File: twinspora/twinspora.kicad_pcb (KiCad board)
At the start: 2 copper layers, 81 parts, among them J1 XY-SH1_0-4A61, J2 TYPE-C-31-M-12, J3 XY-SH1_0-6A51, J4 XY-SH1_0-6A51, J5 XY-XH2_54-2A21, J6 XY-XH2_54-2A21, J7 XY-XH2_54-3A11, Q1 AO3401A, U1 STM32G473RBTx, U10 DRV8316CRRGFR, U2 MT6701QT, U3 MT6701QT, U5 DRV8316CRRGFR, U6 TS1187A26020, U7 CA-IF1044VD-Q1, U8 XC6206P332MR, U9 TS1187A26020, X2 X322512MSB4SI

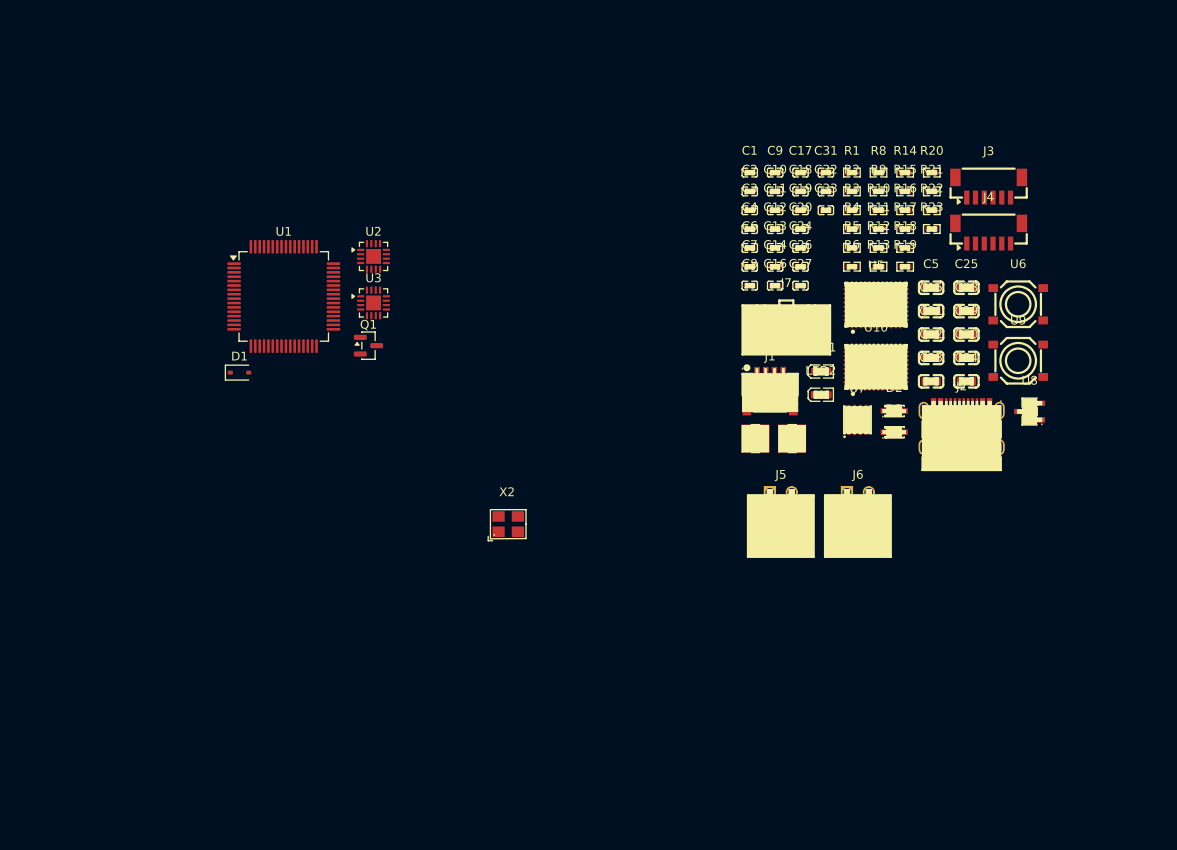
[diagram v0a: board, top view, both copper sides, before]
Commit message: added smt nut
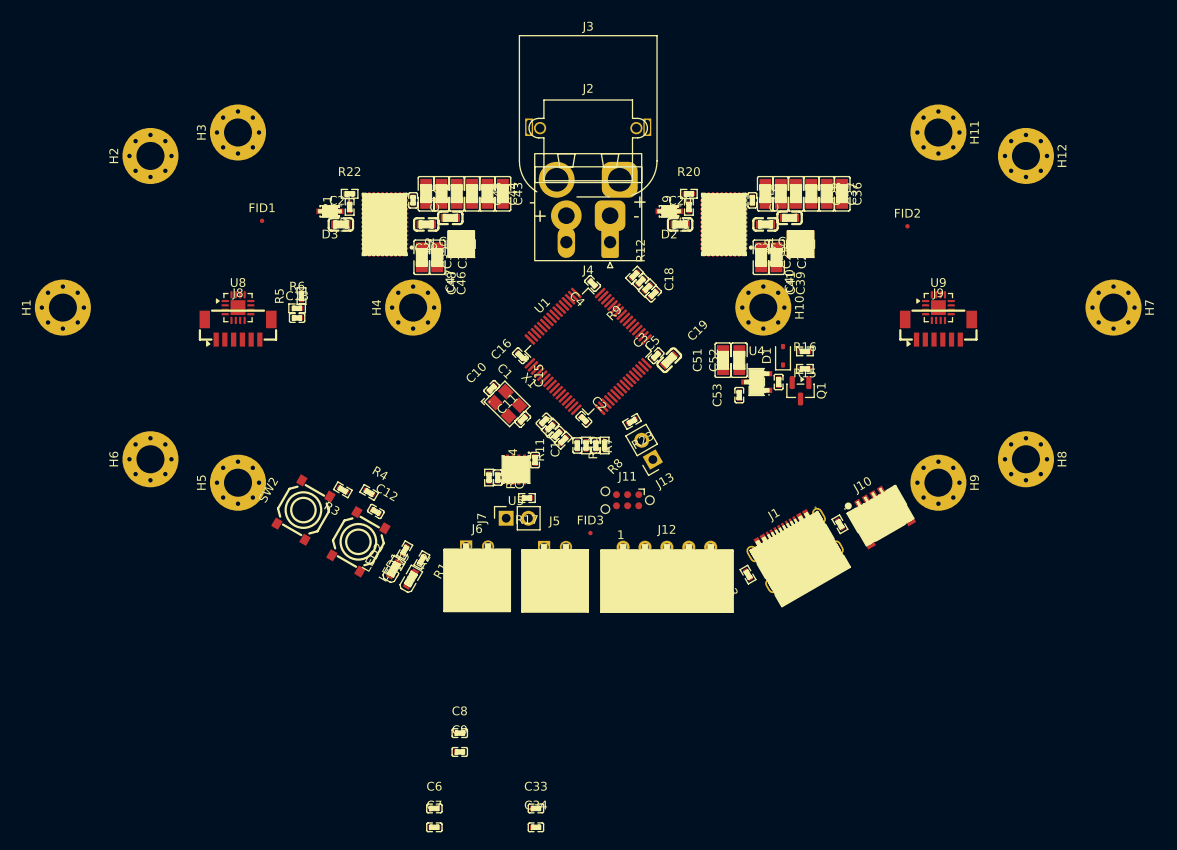
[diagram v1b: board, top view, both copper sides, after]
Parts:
- removed U10: DRV8316CRRGFR, Motor_Driver:VQFN-40_L7.0-W5.0-P0.50-BL-EP5.7
- removed U2, U3: MT6701QT, Package_DFN_QFN:QFN-16-1EP_3x3mm_P0.5mm_EP1.7x1.7mm
- removed X2: X322512MSB4SI, Oscillator:X322512MSB4SI
- added C35: CL05B104KB54PNC, Basic_Capacitors_Resistors:C0402, F.Cu at (158.7, 87.8)
- added C36: GRM21BR61H106KE43L, Basic_Capacitors_Resistors:C0805, F.Cu at (169.0, 87.0)
- added C37: GRM21BR61H106KE43L, Basic_Capacitors_Resistors:C0805, F.Cu at (167.2, 87.0)
- added C38: GRM21BR61H106KE43L, Basic_Capacitors_Resistors:C0805, F.Cu at (165.5, 87.0)
- added C39: GRM21BR61H106KE43L, Basic_Capacitors_Resistors:C0805, F.Cu at (163.7, 87.0)
- added C40: GRM21BR61H106KE43L, Basic_Capacitors_Resistors:C0805, F.Cu at (162.0, 87.0)
- added C41: GRM21BR61H106KE43L, Basic_Capacitors_Resistors:C0805, F.Cu at (160.2, 87.0)
- added C42: CL05B104KB54PNC, Basic_Capacitors_Resistors:C0402, F.Cu at (120.0, 87.8)
- added C43: GRM21BR61H106KE43L, Basic_Capacitors_Resistors:C0805, F.Cu at (130.2, 87.0)
- added C44: GRM21BR61H106KE43L, Basic_Capacitors_Resistors:C0805, F.Cu at (128.5, 87.0)
- added C45: GRM21BR61H106KE43L, Basic_Capacitors_Resistors:C0805, F.Cu at (126.7, 87.0)
- added C46: GRM21BR61H106KE43L, Basic_Capacitors_Resistors:C0805, F.Cu at (125.0, 87.0)
- added C47: GRM21BR61H106KE43L, Basic_Capacitors_Resistors:C0805, F.Cu at (123.2, 87.0)
- added C48: GRM21BR61H106KE43L, Basic_Capacitors_Resistors:C0805, F.Cu at (121.5, 87.0)
- added C51: GRM21BR61H106KE43L, Basic_Capacitors_Resistors:C0805, F.Cu at (155.4, 106.0)
- added C52: GRM21BR61H106KE43L, Basic_Capacitors_Resistors:C0805, F.Cu at (157.3, 106.0)
- added C53: CL05B104KB54PNC, Basic_Capacitors_Resistors:C0402, F.Cu at (157.2, 110.0)
- added FID1: Fiducial, Fiducial:Fiducial_0.5mm_Mask1mm, F.Cu at (102.7, 90.1)
- added FID2: Fiducial, Fiducial:Fiducial_0.5mm_Mask1mm, F.Cu at (176.5, 90.7)
- added FID3: Fiducial, Fiducial:Fiducial_0.5mm_Mask1mm, F.Cu at (140.2, 125.8)
- added H1: MountingHole_Pad, MountingHole:MountingHole_3.2mm_M3_Pad_Via, F.Cu at (80.0, 100.0)
- added H10: MountingHole_Pad, MountingHole:MountingHole_3.2mm_M3_Pad_Via, F.Cu at (160.0, 100.0)
- added H11: MountingHole_Pad, MountingHole:MountingHole_3.2mm_M3_Pad_Via, F.Cu at (180.0, 80.0)
- added H12: MountingHole_Pad, MountingHole:MountingHole_3.2mm_M3_Pad_Via, F.Cu at (190.0, 82.7)
- added H2: MountingHole_Pad, MountingHole:MountingHole_3.2mm_M3_Pad_Via, F.Cu at (90.0, 82.7)
- added H3: MountingHole_Pad, MountingHole:MountingHole_3.2mm_M3_Pad_Via, F.Cu at (100.0, 80.0)
- added H4: MountingHole_Pad, MountingHole:MountingHole_3.2mm_M3_Pad_Via, F.Cu at (120.0, 100.0)
- added H5: MountingHole_Pad, MountingHole:MountingHole_3.2mm_M3_Pad_Via, F.Cu at (100.0, 120.0)
- added H6: MountingHole_Pad, MountingHole:MountingHole_3.2mm_M3_Pad_Via, F.Cu at (90.0, 117.3)
- added H7: MountingHole_Pad, MountingHole:MountingHole_3.2mm_M3_Pad_Via, F.Cu at (200.0, 100.0)
- added H8: MountingHole_Pad, MountingHole:MountingHole_3.2mm_M3_Pad_Via, F.Cu at (190.0, 117.3)
- added H9: MountingHole_Pad, MountingHole:MountingHole_3.2mm_M3_Pad_Via, F.Cu at (180.0, 120.0)
- added J10: XY-SH1_0-4A61, Connector_SH1.0:CONN-SMD_4P-P1.00-WT, F.Cu at (173.2, 123.5)
- added J11: ~, Connector:Tag-Connect_TC2030-IDC-NL, F.Cu at (144.5, 122.0)
- added J12: XY-XH2_54-5A21, Connector_XH2.54:HDR-TH_5P-P2.50-H-F-W7.0-N, F.Cu at (149.0, 127.4)
- added J13: Conn_01x02, Connector_PinSocket_2.54mm:PinSocket_1x02_P2.54mm_Vertical, F.Cu at (147.4, 117.3)
- added J8: XY-SH1_0-6A51, Connector_SH1.0:CONN-SMD_6P-P1.00_XY-SH1.0-6A51, F.Cu at (100.0, 102.5)
- added J9: XY-SH1_0-6A51, Connector_SH1.0:CONN-SMD_6P-P1.00_XY-SH1.0-6A51, F.Cu at (180.0, 102.5)
- added R7: 0402WGF499JTCE, Basic_Capacitors_Resistors:R0402, F.Cu at (139.8, 115.8)
- added SW2: TS1187A26020, Switch:SW-SMD_4P-L5.2-W5.2-1, F.Cu at (107.5, 123.1)
- added SW3: TS1187A26020, Switch:SW-SMD_4P-L5.2-W5.2-1, F.Cu at (113.8, 126.8)
- added U4: XC6206P332MR, Regulator_Linear:SOT-23-3_L2.9-W1.6-P1.90-LS2.8-BR, F.Cu at (159.2, 108.5)
- added X1: X322512MSB4SI, Oscillator:X322512MSB4SI, F.Cu at (130.8, 111.0)
- C10, C11: value CL05B104KB54PNC -> 0402CG200J500NT
- C13, C7, C9: value CL05B104KB54PNC -> CL05A105KA5NQNC
- C14, C6: value CL05A105KA5NQNC -> CL05B103KB5NNNC
- C15: value CL10A226MQ8NRNC -> CL05B103KB5NNNC; footprint Basic_Capacitors_Resistors:C0603 -> Basic_Capacitors_Resistors:C0402
- C16, C17, C18, C19: value CL05B104KB54PNC -> CL05B103KB5NNNC
- C2, C3: value 0402CG200J500NT -> CL05B104KB54PNC
- C20: value CL05A105KA5NQNC -> CL10A105KB8NNNC; footprint Basic_Capacitors_Resistors:C0402 -> Basic_Capacitors_Resistors:C0603
- C21, C30: value CL10A226MQ8NRNC -> CL10A105KB8NNNC
- C22, C23, C34: value CL10A226MQ8NRNC -> CL05B104KB54PNC; footprint Basic_Capacitors_Resistors:C0603 -> Basic_Capacitors_Resistors:C0402
- C24: value CL05A105KA5NQNC -> CL05B104KB54PNC
- C25, C29: value CL10A226MQ8NRNC -> CL10B473KB8NNNC
- C26: value CL05B104KB54PNC -> CL10A105KB8NNNC; footprint Basic_Capacitors_Resistors:C0402 -> Basic_Capacitors_Resistors:C0603
- C27, C31, C32: value CL05A105KA5NQNC -> GRM21BR61H106KE43L; footprint Basic_Capacitors_Resistors:C0402 -> Basic_Capacitors_Resistors:C0805
- C28: value CL10A226MQ8NRNC -> GRM21BR61H106KE43L; footprint Basic_Capacitors_Resistors:C0603 -> Basic_Capacitors_Resistors:C0805
- C4: value CL05B103KB5NNNC -> CL05B104KB54PNC
- D2, D3: value BZT52B5V1S_C19077434 -> BZT52B5V1S
- J1: value XY-SH1_0-4A61 -> TYPE-C-31-M-12; footprint Connector_SH1.0:CONN-SMD_4P-P1.00-WT -> Connector_USB:USB-C_SMD-TYPE-C-31-M-12_1
- J2: value TYPE-C-31-M-12 -> XT30U-M; footprint Connector_USB:USB-C_SMD-TYPE-C-31-M-12_1 -> Connector_AMASS:AMASS_XT30PW-M_1x02_P2.50mm_Horizontal
- J3: value XY-SH1_0-6A51 -> XT60PW-M; footprint Connector_SH1.0:CONN-SMD_6P-P1.00_XY-SH1.0-6A51 -> Connector_AMASS:AMASS_XT60PW-M_1x02_P7.20mm_Horizontal
- J4: value XY-SH1_0-6A51 -> Conn_01x02; footprint Connector_SH1.0:CONN-SMD_6P-P1.00_XY-SH1.0-6A51 -> Connector_Phoenix_MSTB:PhoenixContact_MSTBA_2,5_2-G_1x02_P5.00mm_Horizontal
- J7: value XY-XH2_54-3A11 -> Conn_01x02; footprint Connector_XH2.54:HDR-TH_3P-P2.50-V-F-2 -> Connector_PinSocket_2.54mm:PinSocket_1x02_P2.54mm_Vertical
- LED1: value KT-0603R -> KT-0603W; footprint LED:LED0603-RD -> LED:LED0603-R-RD_WHITE
- LED2: value KT-0603W -> KT-0603R; footprint LED:LED0603-R-RD_WHITE -> LED:LED0603-RD
- R10: value 0402WGF1002TCE -> 0402WGF499JTCE
- R11: value 0402WGF1003TCE -> 0402WGF499JTCE
- R12, R9: value 0402WGF5101TCE -> 0402WGF499JTCE
- R14: value 0402WGF3300TCE -> 0402WGF5101TCE
- R16, R23, R6: value 0402WGF3300TCE -> 0402WGF1002TCE
- R17: value 0402WGF1003TCE -> 0402WGF1200TCE
- R18: value 0402WGF5101TCE -> 0402WGF1002TCE
- R19, R21: value 0402WGF3300TCE -> 0402WGF1003TCE
- R2: value 0402WGF1002TCE -> 0402WGF3300TCE
- R20: value 0402WGF1003TCE -> 0402WGF5101TCE
- R3: value 0402WGF1002TCE -> 0402WGF5101TCE
- R4: value 0402WGF1200TCE -> 0402WGF1002TCE
- R5: value 0402WGF1002TCE -> 0402WGF1003TCE
- R8: value 0402WGF3300TCE -> 0402WGF499JTCE
- U5: value DRV8316CRRGFR -> CA-IF1044VD-Q1; footprint Motor_Driver:VQFN-40_L7.0-W5.0-P0.50-BL-EP5.7 -> Interface_CAN_LIN:DFN-8_L3.0-W3.0-P0.65-BL-EP2.45
- U6: value TS1187A26020 -> DRV8316CRRGFR; footprint Switch:SW-SMD_4P-L5.2-W5.2-1 -> Motor_Driver:VQFN-40_L7.0-W5.0-P0.50-BL-EP5.7
- U7: value CA-IF1044VD-Q1 -> DRV8316CRRGFR; footprint Interface_CAN_LIN:DFN-8_L3.0-W3.0-P0.65-BL-EP2.45 -> Motor_Driver:VQFN-40_L7.0-W5.0-P0.50-BL-EP5.7
- U8: value XC6206P332MR -> MT6701QT; footprint Regulator_Linear:SOT-23-3_L2.9-W1.6-P1.90-LS2.8-BR -> Package_DFN_QFN:QFN-16-1EP_3x3mm_P0.5mm_EP1.7x1.7mm
- U9: value TS1187A26020 -> MT6701QT; footprint Switch:SW-SMD_4P-L5.2-W5.2-1 -> Package_DFN_QFN:QFN-16-1EP_3x3mm_P0.5mm_EP1.7x1.7mm
- moved U8 91.2 mm to (100.0, 100.0)
- moved C33 75.9 mm to (134.0, 157.2)
- moved C9 75.3 mm to (125.3, 150.8)
- moved C7 73.5 mm to (122.4, 159.4)
- moved C6 73.5 mm to (122.4, 157.2)
- moved C34 70.8 mm to (134.0, 159.4)
- moved D3 69.2 mm to (110.5, 89.0), turned to 180 degrees
- moved C21 68.6 mm to (111.8, 90.5)
- moved R22 66.5 mm to (112.8, 87.0)
- moved R21 66.5 mm to (112.8, 88.5), turned to 90 degrees
- moved R3 66.3 mm to (112.0, 120.8), turned to 150 degrees
- moved R1 66.1 mm to (121.0, 128.8), turned to -120 degrees
- moved R2 65.5 mm to (119.1, 127.7), turned to -120 degrees
- moved R6 63.5 mm to (106.8, 100.1)
- moved R5 63.1 mm to (107.2, 98.7), turned to 90 degrees
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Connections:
- C1 pad 1: GND -> +3.3V
- C1 pad 2: /RESET -> GND
- C10 pad 1: +3.3V -> /RCC_OSC_IN
- C11 pad 2: +3.3V -> /RCC_OSC_OUT
- C12 pad 2: +3.3V -> /RESET
- C13 pad 1: +3.3V -> GND
- C13 pad 2: GND -> /VSENS
- C14 pad 1: +3.3V -> GND
- C14 pad 2: GND -> /ADC1_IN3
- C15 pad 2: +3.3V -> /ADC1_IN4
- C16 pad 2: +3.3V -> /ADC2_IN1
- C17 pad 2: +5V -> /ADC2_IN2
- C18 pad 2: /CAN_VIO -> /ADC5_IN1
- C19 pad 2: +5V -> /ADC5_IN2
- C2 pad 1: /RCC_OSC_IN -> +3.3V
- C20 pad 2: Net-(C20-Pad2) -> Net-(U6-AVDD)
- C21 pad 2: /ADC5_IN1 -> Net-(U7-AVDD)
- C22 pad 2: /ADC2_IN1 -> +5V
- C23 pad 2: /ADC1_IN2 -> /CAN_VIO
- C24 pad 2: Net-(U5-AVDD) -> +5V
- C25 pad 1: GND -> Net-(U6-CPL)
- C25 pad 2: /BUCK -> Net-(U6-CPH)
- C26 pad 1: Net-(U5-CPH) -> VCC
- C26 pad 2: Net-(U5-CPL) -> Net-(U6-CP)
- C27 pad 1: Net-(U5-CP) -> /BUCK
- C27 pad 2: VBUS -> GND
- C28 pad 1: GND -> /BUCK
- C28 pad 2: /ADC1_IN3 -> GND
- C29 pad 1: GND -> Net-(U7-CPL)
- C29 pad 2: /ADC2_IN9 -> Net-(U7-CPH)
- C3 pad 1: GND -> +3.3V
- C3 pad 2: /RCC_OSC_OUT -> GND
- C30 pad 1: GND -> VCC
- C30 pad 2: /ADC5_IN2 -> Net-(U7-CP)
- C31 pad 1: GND -> /5V_BKOUT
- C31 pad 2: Net-(U10-AVDD) -> GND
- C32 pad 1: Net-(U10-CP) -> /5V_BKOUT
- C32 pad 2: VBUS -> GND
- C33 pad 1: Net-(U10-CPH) -> GND
- C33 pad 2: Net-(U10-CPL) -> +3.3V
- C34 pad 2: /BUCK -> +3.3V
- D2 pad 1: /NSLEEP -> Net-(D2-K)
- D3 pad 1: /NSLEEP -> Net-(D3-K)
- J1 pad 2: +3.3V -> GND
- J1 pad 3: /I2C_SDA -> GND
- J1 pad 4: /I2C_SCL -> GND
- J2 pad 2: GND -> VCC
- J3 pad 2: +3.3V -> VCC
- J3 pad 3: /SPI3_NSS -> GND
- J3 pad 4: /SPI3_SCK -> GND
- J4 pad 2: +3.3V -> VCC
- J7 pad 1: /GPIO1 -> /CAN_L
- J7 pad 2: /GPIO2 -> Net-(J7-Pin_2)
- L1 pad 1: Net-(U5-SW_BK) -> /BUCK
- L1 pad 2: /BUCK -> Net-(U6-SW_BK)
- L2 pad 1: Net-(U10-SW_BK) -> /5V_BKOUT
- L2 pad 2: /BUCK -> Net-(U7-SW_BK)
- LED1 pad 1: GND -> Net-(LED1-A)
- LED1 pad 2: Net-(LED1-A) -> GND
- LED2 pad 1: Net-(LED2-A) -> GND
- LED2 pad 2: GND -> Net-(LED2-A)
- R1 pad 1: GND -> +3.3V
- R1 pad 2: /BOOT -> Net-(LED1-A)
- R10 pad 1: GND -> /ADC1_IN4
- R10 pad 2: Net-(C20-Pad2) -> /SOA2
- R11 pad 1: Net-(C20-Pad2) -> /ADC2_IN2
- R11 pad 2: VBUS -> /SOB2
- R12 pad 1: /CC1 -> /ADC5_IN2
- R12 pad 2: GND -> /SOC2
- R13 pad 1: /CC2 -> /CC1
- R14 pad 1: Net-(U5-SOC) -> /CC2
- R14 pad 2: /ADC5_IN1 -> GND
- R15 pad 1: Net-(U5-SOB) -> Net-(Q1-G)
- R15 pad 2: /ADC2_IN1 -> VBUS
- R16 pad 1: Net-(U5-SOA) -> GND
- R16 pad 2: /ADC1_IN2 -> Net-(Q1-G)
- R17 pad 1: /NSLEEP -> /CAN_H
- R17 pad 2: VBUS -> Net-(J7-Pin_2)
- R18 pad 1: /NFAULT -> GND
- R18 pad 2: +3.3V -> /CAN_VIO
- R19 pad 1: Net-(U10-SOA) -> Net-(D2-K)
- R19 pad 2: /ADC1_IN3 -> VCC
- R2 pad 1: +3.3V -> /USER_LED
- R2 pad 2: Net-(R2-Pad2) -> Net-(LED2-A)
- R20 pad 1: /NSLEEP -> +3.3V
- R20 pad 2: VBUS -> Net-(U6-nFAULT)
- R21 pad 1: Net-(U10-SOB) -> Net-(D3-K)
- R21 pad 2: /ADC2_IN9 -> VCC
- R22 pad 1: /NFAULT -> +3.3V
- R22 pad 2: +3.3V -> Net-(U7-nFAULT)
- R23 pad 1: Net-(U10-SOC) -> /I2C_SDA
- R23 pad 2: /ADC5_IN2 -> Net-(J13-Pin_2)
- R3 pad 2: Net-(Q1-G) -> /BOOT
- R4 pad 1: /CAN_H -> /RESET
- R4 pad 2: /CAN_L -> +3.3V
- R5 pad 1: GND -> /VSENS
- R5 pad 2: /CAN_VIO -> VCC
- R6 pad 1: Net-(Q1-G) -> GND
- R6 pad 2: VBUS -> /VSENS
- R8 pad 1: /USER_LED -> /ADC2_IN1
- R8 pad 2: Net-(LED1-A) -> /SOB1
- R9 pad 1: +3.3V -> /ADC5_IN1
- R9 pad 2: Net-(LED2-A) -> /SOC1
- U1 pad 11: /ADC2_IN9 -> /VSENS
- U1 pad 13: /ADC1_IN2 -> /ADC2_IN2
- U1 pad 17: /VSENS -> /ADC1_IN4
- U5 pad 1: unconnected-(U5-NC-Pad1) -> +5V
- U5 pad 2: GND -> /FDCAN_TX
- U5 pad 3: /BUCK -> /FDCAN_RX
- U5 pad 5: Net-(U5-SW_BK) -> /CAN_VIO
- U5 pad 6: Net-(U5-CPL) -> /CAN_L
- U5 pad 7: Net-(U5-CPH) -> /CAN_H
- U5 pad 8: Net-(U5-CP) -> GND
- U5 pad 9: VBUS -> GND
- U6 pad 1: +3.3V -> unconnected-(U6-NC-Pad1)
- U6 pad 2: +3.3V -> GND
- U6 pad 3: /BOOT -> /BUCK
- U6 pad 4: /BOOT -> GND
- U7 pad 2: unconnected-(U7-GND-Pad2) -> GND
- U7 pad 3: unconnected-(U7-VCC-Pad3) -> /5V_BKOUT
- U7 pad 4: unconnected-(U7-RXD-Pad4) -> GND
- U7 pad 5: /CAN_VIO -> Net-(U7-SW_BK)
- U7 pad 6: /CAN_L -> Net-(U7-CPL)
- U7 pad 7: /CAN_H -> Net-(U7-CPH)
- U7 pad 8: GND -> Net-(U7-CP)
- U7 pad 9: unconnected-(U7-EP-Pad9) -> VCC
- U8 pad 1: GND -> unconnected-(U8-NC-Pad1)
- U8 pad 2: +5V -> unconnected-(U8-NC-Pad2)
- U8 pad 3: +3.3V -> unconnected-(U8-NC-Pad3)
- U9 pad 1: Net-(R2-Pad2) -> unconnected-(U9-NC-Pad1)
- U9 pad 2: /RESET -> unconnected-(U9-NC-Pad2)
- U9 pad 3: GND -> unconnected-(U9-NC-Pad3)
- U9 pad 4: GND -> unconnected-(U9-NC-Pad4)
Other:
- copper layers 2 -> 4

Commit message: initial completion
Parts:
- removed H10, H11, H12, H5, H6, H7, H8, H9: MountingHole_Pad, MountingHole:MountingHole_3.2mm_M3_Pad_Via
- added C49: 0402CG470J500NT, Basic_Capacitors_Resistors:C0402, F.Cu at (98.2, 129.6)
- added C50: 0402CG470J500NT, Basic_Capacitors_Resistors:C0402, F.Cu at (96.8, 128.2)
- added H13: SMTSOM225BTR, Mechanical:SMD_BD5.6-D3.6, F.Cu at (80.0, 105.8)
- added H14: SMTSOM225BTR, Mechanical:SMD_BD5.6-D3.6, F.Cu at (80.0, 134.2)
- added H15: SMTSOM225BTR, Mechanical:SMD_BD5.6-D3.6, F.Cu at (150.0, 134.2)
- added H16: SMTSOM225BTR, Mechanical:SMD_BD5.6-D3.6, F.Cu at (150.0, 105.8)
- added J14: Conn_01x03, Connector_DORABO:CONN-TH_DB125-2.54-3P-GN, F.Cu at (134.8, 103.1)
- added J15: Conn_01x03, Connector_DORABO:CONN-TH_DB125-2.54-3P-GN, F.Cu at (91.5, 103.1)
- added R24: 0402WGF1200TCE, Basic_Capacitors_Resistors:R0402, F.Cu at (141.6, 130.5)
- added R25: 0402WGF1200TCE, Basic_Capacitors_Resistors:R0402, F.Cu at (142.9, 130.5)
- added R26: 0603WAF0000T5E, Basic_Capacitors_Resistors:R0603, F.Cu at (133.0, 124.0)
- added R27: 0603WAF0000T5E, Basic_Capacitors_Resistors:R0603, F.Cu at (94.2, 123.0)
- added R28: 0603WAF0000T5E, Basic_Capacitors_Resistors:R0603, F.Cu at (134.8, 124.0)
- added R29: 0603WAF0000T5E, Basic_Capacitors_Resistors:R0603, F.Cu at (97.2, 123.0)
- added R30: 0603WAF0000T5E, Basic_Capacitors_Resistors:R0603, F.Cu at (136.5, 124.0)
- added R31: 0603WAF0000T5E, Basic_Capacitors_Resistors:R0603, F.Cu at (99.5, 122.2)
- added TP1: ~, TestPoint:TestPoint_Pad_D1.0mm, F.Cu at (101.8, 118.2)
- added TP10: ~, TestPoint:TestPoint_Pad_D1.0mm, F.Cu at (143.2, 120.2)
- added TP11: ~, TestPoint:TestPoint_Pad_D1.0mm, F.Cu at (143.2, 124.2)
- added TP12: ~, TestPoint:TestPoint_Pad_D1.0mm, F.Cu at (143.2, 122.2)
- added TP13: ~, TestPoint:TestPoint_Pad_D1.0mm, F.Cu at (131.2, 118.8)
- added TP14: ~, TestPoint:TestPoint_Pad_D1.0mm, F.Cu at (129.5, 119.8)
- added TP15: ~, TestPoint:TestPoint_Pad_D1.0mm, F.Cu at (131.2, 116.8)
- added TP16: ~, TestPoint:TestPoint_Pad_D1.0mm, F.Cu at (129.5, 117.8)
- added TP17: ~, TestPoint:TestPoint_Pad_D1.0mm, F.Cu at (123.8, 130.5)
- added TP18: ~, TestPoint:TestPoint_Pad_D1.0mm, F.Cu at (125.8, 130.5)
- added TP19: ~, TestPoint:TestPoint_Pad_D1.0mm, F.Cu at (120.6, 115.1)
- added TP2: ~, TestPoint:TestPoint_Pad_D1.0mm, F.Cu at (103.5, 119.2)
- added TP20: ~, TestPoint:TestPoint_Pad_D1.0mm, F.Cu at (105.2, 115.0)
- added TP21: ~, TestPoint:TestPoint_Pad_D1.0mm, F.Cu at (122.0, 116.5)
- added TP22: ~, TestPoint:TestPoint_Pad_D1.0mm, F.Cu at (105.2, 117.0)
- added TP23: ~, TestPoint:TestPoint_Pad_D1.0mm, F.Cu at (105.0, 129.0)
- added TP24: ~, TestPoint:TestPoint_Pad_D1.0mm, F.Cu at (104.0, 130.8)
- added TP25: ~, TestPoint:TestPoint_Pad_D1.0mm, F.Cu at (85.0, 125.3)
- added TP26: ~, TestPoint:TestPoint_Pad_D1.0mm, F.Cu at (81.5, 120.2)
- added TP27: ~, TestPoint:TestPoint_Pad_D1.0mm, F.Cu at (83.0, 127.5)
- added TP28: ~, TestPoint:TestPoint_Pad_D1.0mm, F.Cu at (107.2, 113.5)
- added TP29: ~, TestPoint:TestPoint_Pad_D1.0mm, F.Cu at (146.0, 122.0)
- added TP3: ~, TestPoint:TestPoint_Pad_D1.0mm, F.Cu at (101.8, 120.2)
- added TP30: ~, TestPoint:TestPoint_Pad_D1.0mm, F.Cu at (146.0, 124.0)
- added TP31: ~, TestPoint:TestPoint_Pad_D1.0mm, F.Cu at (129.5, 115.8)
- added TP32: ~, TestPoint:TestPoint_Pad_D1.0mm, F.Cu at (127.5, 115.8)
- added TP33: ~, TestPoint:TestPoint_Pad_D1.0mm, F.Cu at (128.5, 114.0)
- added TP34: ~, TestPoint:TestPoint_Pad_D1.0mm, F.Cu at (125.5, 115.8)
- added TP35: ~, TestPoint:TestPoint_Pad_D1.0mm, F.Cu at (126.5, 114.0)
- added TP36: ~, TestPoint:TestPoint_Pad_D1.0mm, F.Cu at (124.5, 114.0)
- added TP37: ~, TestPoint:TestPoint_Pad_D1.0mm, F.Cu at (90.5, 117.8)
- added TP38: ~, TestPoint:TestPoint_Pad_D1.0mm, F.Cu at (89.5, 116.0)
- added TP39: ~, TestPoint:TestPoint_Pad_D1.0mm, F.Cu at (88.5, 114.2)
- added TP4: ~, TestPoint:TestPoint_Pad_D1.0mm, F.Cu at (103.5, 121.2)
- added TP40: ~, TestPoint:TestPoint_Pad_D1.0mm, F.Cu at (88.5, 117.8)
- added TP41: ~, TestPoint:TestPoint_Pad_D1.0mm, F.Cu at (87.5, 116.0)
- added TP42: ~, TestPoint:TestPoint_Pad_D1.0mm, F.Cu at (86.5, 114.3)
- added TP43: ~, TestPoint:TestPoint_Pad_D1.0mm, F.Cu at (127.8, 130.5)
- added TP5: ~, TestPoint:TestPoint_Pad_D1.0mm, F.Cu at (87.0, 119.2)
- added TP6: ~, TestPoint:TestPoint_Pad_D1.0mm, F.Cu at (87.0, 125.2)
- added TP7: ~, TestPoint:TestPoint_Pad_D1.0mm, F.Cu at (87.0, 121.2)
- added TP8: ~, TestPoint:TestPoint_Pad_D1.0mm, F.Cu at (87.0, 123.2)
- added TP9: ~, TestPoint:TestPoint_Pad_D1.0mm, F.Cu at (143.2, 118.2)
- added U10: SRV05-4A, Package_TO_SOT_SMD:SOT-23-6, F.Cu at (135.0, 127.5)
- added U11: SRV05-4A, Package_TO_SOT_SMD:SOT-23-6, F.Cu at (94.9, 125.8)
- added U12: SRV05-4A, Package_TO_SOT_SMD:SOT-23-6, F.Cu at (86.5, 128.6)
- added U2: SRV05-4A, Package_TO_SOT_SMD:SOT-23-6, F.Cu at (99.4, 127.0)
- added U3: SRV05-4A, Package_TO_SOT_SMD:SOT-23-6, F.Cu at (144.5, 127.2)
- C6: value CL05B103KB5NNNC -> CL05B104KB54PNC
- J12: value XY-XH2_54-5A21 -> XY-SH1_0-5A61; footprint Connector_XH2.54:HDR-TH_5P-P2.50-H-F-W7.0-N -> Connector_SH1.0:CONN-SMD_5P-P1.00_XYECONN_XY-SH1.0-5A61
- J5, J6: value XY-XH2_54-2A21 -> XY-SH1_0-3A61; footprint Connector_XH2.54:HDR-TH_2P-P2.50_XY-XH2.54-2A21 -> Connector_SH1.0:CONN-SMD_3P-P1.00_XYECONN_XY-SH1.0-3A61
- moved J9 92.1 mm to (90.4, 123.5), turned to -90 degrees
- moved U9 87.3 mm to (95.0, 120.0)
- moved R15 86.4 mm to (79.0, 115.5), turned to -90 degrees
- moved R16 84.2 mm to (81.0, 115.5), turned to 90 degrees
- moved D1 83.7 mm to (79.5, 118.0), turned to 180 degrees
- moved Q1 81.0 mm to (83.5, 116.0), turned to 0 degrees
- moved C22 78.9 mm to (83.5, 118.5), turned to 180 degrees
- moved C52 77.6 mm to (81.5, 123.0), turned to 180 degrees
- moved U4 76.3 mm to (84.0, 121.0), turned to 90 degrees
- moved C51 76.3 mm to (81.5, 124.9), turned to 180 degrees
- moved H3 73.8 mm to (150.0, 134.2), turned to 180 degrees
- moved C53 73.7 mm to (84.8, 123.5), turned to 180 degrees
- moved R14 68.2 mm to (100.8, 129.5), turned to -45 degrees
- moved J1 66.4 mm to (97.4, 134.0), turned to 0 degrees
- moved R13 63.3 mm to (95.0, 129.2), turned to 180 degrees
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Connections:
- C27 pad 1: /BUCK -> /5V_BKOUT
- C28 pad 1: /BUCK -> /5V_BKOUT
- C31 pad 1: /5V_BKOUT -> /BUCK
- C32 pad 1: /5V_BKOUT -> /BUCK
- J10 pad 3: /I2C_SDA -> Net-(J10-Pad3)
- J10 pad 4: /I2C_SCL -> Net-(J10-Pad4)
- J12 pad 1: GND -> /GPIO3
- J12 pad 2: /5V_BKOUT -> /GPIO2
- J12 pad 4: /GPIO2 -> /5V_BKOUT
- J12 pad 5: /GPIO3 -> GND
- J5 pad 1: /CAN_H -> GND
- J6 pad 1: /CAN_H -> GND
- J8 pad 5: /SPI3_SCK -> /SPI3_NSS
- J8 pad 6: /SPI3_NSS -> /SPI3_SCK
- J9 pad 5: /SPI2_SCK -> /SPI2_NSS
- J9 pad 6: /SPI2_NSS -> /SPI2_SCK
- L1 pad 1: /BUCK -> /5V_BKOUT
- L2 pad 1: /5V_BKOUT -> /BUCK
- U6 pad 3: /BUCK -> /5V_BKOUT
- U7 pad 3: /5V_BKOUT -> /BUCK
- U8 pad 6: /SPI3_MISO -> Net-(U8-A)
- U8 pad 7: /SPI3_SCK -> Net-(U8-B)
- U8 pad 8: /SPI3_NSS -> Net-(U8-Z)
- U9 pad 6: /SPI2_MISO -> Net-(U9-A)
- U9 pad 7: /SPI2_SCK -> Net-(U9-B)
- U9 pad 8: /SPI2_NSS -> Net-(U9-Z)
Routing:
- net +5V: track 0.00 -> 97.8 mm, vias 0 -> 5
- net /5V_BKOUT: track 0.00 -> 90.8 mm, vias 0 -> 4
- net +3.3V: track 0.00 -> 85.9 mm, vias 0 -> 41
- net GND: track 0.00 -> 61.5 mm, vias 0 -> 297
- net /I2C_SDA: track 0.00 -> 52.8 mm, vias 0 -> 3
- net /GPIO1: track 0.00 -> 49.0 mm, vias 0 -> 2
- net /SOC1: track 0.00 -> 47.3 mm, vias 0 -> 2
- net /RESET: track 0.00 -> 46.4 mm, vias 0 -> 2
- net /TIM8_CH1N: track 0.00 -> 45.4 mm, vias 0 -> 2
- net /GPIO2: track 0.00 -> 45.4 mm, vias 0 -> 2
- net /TIM8_CH1: track 0.00 -> 44.6 mm, vias 0 -> 2
- net /SPI2_NSS: track 0.00 -> 43.1 mm, vias 0 -> 4
- net VBUS: track 0.00 -> 42.9 mm, vias 0 -> 4
- net /BOOT: track 0.00 -> 42.3 mm, vias 0 -> 2
- net /TIM8_CH2N: track 0.00 -> 42.0 mm, vias 0 -> 2
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- added copper zone on F.Cu, net +3.3V
- added copper zone on In2.Cu, net +3.3V
- added copper zone on F.Cu, net +5V
- added copper zone on F.Cu, net /5V_BKOUT
- added copper zone on F.Cu, net /BUCK
- added copper zone on F.Cu, net /PHA1
- added copper zone on F.Cu, net /PHA2
- added copper zone on F.Cu, net /PHB1
- added copper zone on F.Cu, net /PHB2
- added copper zone on F.Cu, net /PHC1
- added copper zone on F.Cu, net /PHC2
- added copper zone on B.Cu, net GND
- added copper zone on F.Cu, net GND
- added copper zone on In1.Cu, net GND
- added copper zone on In2.Cu, net GND
- added copper zone on B.Cu, net VCC
- added copper zone on F.Cu, net VCC
- added copper zone on In2.Cu, net VCC
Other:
- board outline added: 76.9 x 36.8 mm

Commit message: designators
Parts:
- moved TP29 0.75 mm to (146.8, 122.0)
- moved FID3 0.47 mm to (124.8, 136.8)
- moved C19 0.27 mm to (107.6, 131.5)
- moved TP5 0.24 mm to (87.2, 119.4)
- moved TP6 0.24 mm to (87.2, 125.4)
- moved TP7 0.24 mm to (87.2, 121.4)
- moved TP8 0.24 mm to (87.2, 123.4)
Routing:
- net /I2C_SDA: track 52.8 -> 53.5 mm
- net VCC: track 31.5 -> 32.1 mm
- net GND: vias 297 -> 302

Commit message: final designator edits
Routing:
- net GND: vias 302 -> 304
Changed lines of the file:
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@@
 		(tags "C0402 footprint C1567")
 		(property "Reference" "C24"
-			(at -2.25 0 0)
+			(at -2.164 -0.506 0)
 			(layer "F.SilkS")
 			(effects
@@
 		(tags "C0402 footprint C1567")
 		(property "Reference" "C4"
-			(at 1.041213 -1.080106 135)
+			(at 1.782261 -0.548361 135)
 			(layer "F.SilkS")
 			(effects
@@
 		(tags "R0402 footprint C25120")
 		(property "Reference" "R16"
-			(at -0.000001 -0.999999 90)
+			(at 2.197497 -0.189999 90)
 			(layer "F.SilkS")
 			(effects
@@
 		(tags "R0402 footprint C25120")
 		(property "Reference" "R15"
-			(at -0.000001 1.000001 90)
+			(at -2.197499 0.190001 90)
 			(layer "F.SilkS")
 			(effects
@@
 		(tags "SOD-323_L1.7-W1.3-LS2.6-RD footprint C19077434")
 		(property "Reference" "D3"
-			(at 2.250128 0.027377 0)
+			(at 2.110128 0.019377 90)
 			(layer "F.SilkS")
 			(effects
@@
 	)
 	(via
+		(at 95.574 132.888)
+		(size 0.45)
+		(drill 0.3)
+		(layers "F.Cu" "B.Cu")
+		(free yes)
+		(net "GND")
+	)
+	(via
 		(at 91 129.8)
 		(size 0.45)
@@
 		(net "GND")
 	)
+	(via
+		(at 98.622 132.888)
+		(size 0.45)
+		(drill 0.3)
+		(layers "F.Cu" "B.Cu")
+		(free yes)
+		(net "GND")
+	)
